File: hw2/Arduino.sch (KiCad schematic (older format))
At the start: 9 parts

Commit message: Schematic almost complete
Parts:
- added C? (x5): C, symbol C
- added D? (x2): LED, symbol LED
- added F?: Fuse, symbol Fuse
- added P?: USB_B, symbol USB_B
- added P? (x2): CONN_01X12, symbol CONN_01X12
- added R? (x5): R, symbol R
- added U?: ATmega32U4, symbol ATmega32U4
- gave numbers to parts that had none: 9
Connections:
- net GND: now also C?.2, C?.2, C?.2, C?.2, C?.2, P?.10 (P10), P?.2 (P2), P?.4 (GND), P?.9 (P9), U?.15 (GND), U?.23 (GND), U?.33 ((~HWB~)PE2), U?.35 (GND), U?.43 (GND)
- net VCC: now also D?.2 (A), D?.2 (A), P?.4 (P4), R?.1, U?.14 (VCC), U?.24 (AVCC), U?.34 (VCC), U?.44 (AVCC)
- net at JP1.1: now also F?.1; no longer D1.2 (A)
- new net: R?.2, U?.13 (RESET)
- new net: C?.1, U?.16 (XTAL2)
- new net: C?.1, U?.17 (XTAL1)
- new net: R?.1, U?.22 ((XCK1/~CTS~)PD5)
- new net: C?.1, U?.42 (AREF)
- new net: C?.1, U?.6 (UCAP)
- new net: D?.1 (K), R?.2 (x2)
- new net: P?.2 (D-), R?.2
- new net: P?.3 (D+), R?.2
- new net A0: P?.8 (P8), U?.36 ((ADC7/TDI)PF7)
- new net A1: P?.7 (P7), U?.37 ((ADC6/TDO)PF6)
- new net A2: P?.6 (P6), U?.38 ((ADC5/TMS)PF5)
- new net A3: P?.5 (P5), U?.39 ((ADC4/TCK)PF4)
- new net A4: U?.40 ((ADC1)PF1)
- new net A5: U?.41 ((ADC0)PF0)
- new net D+: R?.1
- new net D-: R?.1
- new net D10: P?.12 (P12), U?.30 ((ADC13/OC1B/OC4B/PCINT13)PB6)
- new net D11: U?.12 ((OC0A/OC1C/~RTS~/PCINT7)PB7)
- new net D12: U?.26 ((T1/~OC4D~/ADC9)PD6)
- new net D13: U?.32 ((ICP3/CLK0/OC4A)PC7)
- new net D14: R?.1, U?.8 ((SS/PCINT0)PB0)
- new net D2: P?.8 (P8), U?.19 ((SDA/INT1)PD1)
- new net D3: P?.7 (P7), U?.18 ((OC0B/SCL/INT0)PD0)
- new net D4: P?.6 (P6), U?.25 ((ICP2/ADC8)PD4)
- new net D5: P?.5 (P5), U?.31 ((OC3A/~OC4A~)PC6)
- new net D6: P?.4 (P4), U?.27 ((T0/OC4D/ADC10)PD7)
- new net D7: P?.3 (P3), U?.1 ((INT6/AIN0)PE6)
- new net D8: P?.2 (P2), U?.28 ((ADC11/PCINT4)PB4)
- new net D9: P?.1 (P1), U?.29 ((ADC12/OC1A/~OC4B~/PCINT12)PB5)
- new net MISO: P?.10 (P10), U?.11 ((PDO/MISO/PCINT3)PB3)
- new net MOSI: P?.11 (P11), U?.10 ((PDI/MOSI/PCINT2)PB2)
- new net RESET: P?.3 (P3)
- new net RXI: P?.11 (P11), U?.20 ((RXD/INT2)PD2)
- new net SCK: P?.9 (P9), U?.9 ((SCLK/PCINT1)PB1)
- new net TX0: P?.12 (P12)
- new net TXD: U?.21 ((TXD/INT3)PD3)
- new net UVCC: C?.1, F?.2, P?.1 (VBUS), U?.2 (UVCC)
- no-connect marks 1 -> 2

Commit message: Schema footprint association almost finalized
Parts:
- added 16MHz1: Crystal_Small, Crystals:Crystal_AT310_d3.0mm_l10.0mm_Horizontal, symbol Crystal_Small
- added P1: CONN_01X02, Socket_Strips:Socket_Strip_Angled_1x02_Pitch2.00mm, symbol CONN_01X02
- 0,1uF1: renamed from C4; footprint (none) -> Capacitors_SMD:C_0805
- 0,1uF2, 1uF2, 1uF3, 22pF1, 22pF2: renamed from C?; footprint (none) -> Capacitors_SMD:C_0805
- 10K1, R1, R2: renamed from R?; footprint (none) -> Resistors_SMD:R_0805
- 10uF1: renamed from C1; footprint (none) -> Capacitors_SMD:CP_Elec_3x5.3
- 10uF2: renamed from C2; footprint (none) -> Capacitors_SMD:CP_Elec_3x5.3
- 1K1: renamed from R1; footprint (none) -> Resistors_SMD:R_0805
- 1uF1: renamed from C3; footprint (none) -> Capacitors_SMD:C_0805
- 500mA1: renamed from F?; footprint (none) -> Fuse_Holders_and_Fuses:Fuse_SMD1206_HandSoldering
- D1: footprint (none) -> Diodes_SMD:D_0805
- D2: renamed from D?; value LED -> Yellow; footprint (none) -> LEDs:LED_0805
- D3: renamed from D?; value LED -> Green; footprint (none) -> LEDs:LED_0805
- JP1: footprint (none) -> Pin_Headers:Pin_Header_Straight_1x02_Pitch1.27mm
- P2, P3: renamed from P?; footprint (none) -> Pin_Headers:Pin_Header_Straight_1x12_Pitch1.27mm
- P4: renamed from P?; footprint (none) -> Connectors:USB_B
- R3, R4: renamed from R?; value R -> 330; footprint (none) -> Resistors_SMD:R_0805
- Red1: renamed from D2; footprint (none) -> LEDs:LED_0805
- U1: footprint (none) -> TO_SOT_Packages_SMD:SOT-23
- gave numbers to parts that had none: 1
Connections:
- net D+: now also U2.4 (D+)
- net D-: now also U2.3 (D-)
- net GND: now also U2.5 (UGND), P1.1 (P1)
- net UVCC: now also U2.7 (VBUS)
- net VCC: now also P1.2 (P2)
- net at 22pF2.1, U2.16 (XTAL2): now also 16MHz1.2
- net at 22pF1.1, U2.17 (XTAL1): now also 16MHz1.1

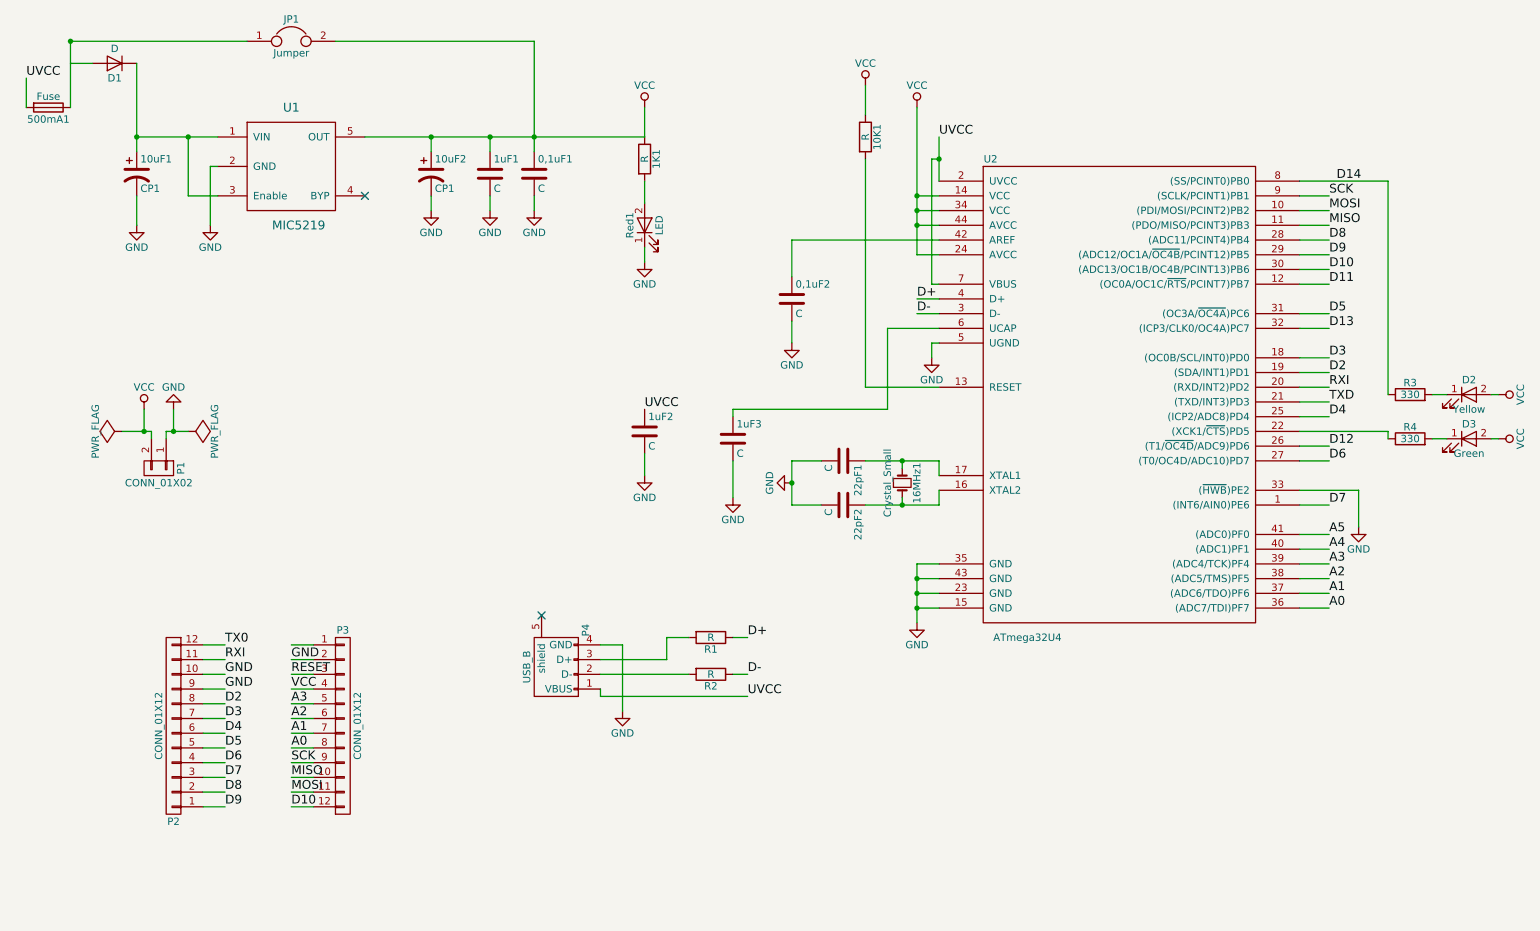
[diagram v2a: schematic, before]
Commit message: Corrections in schema; pcb layout implementation initialized
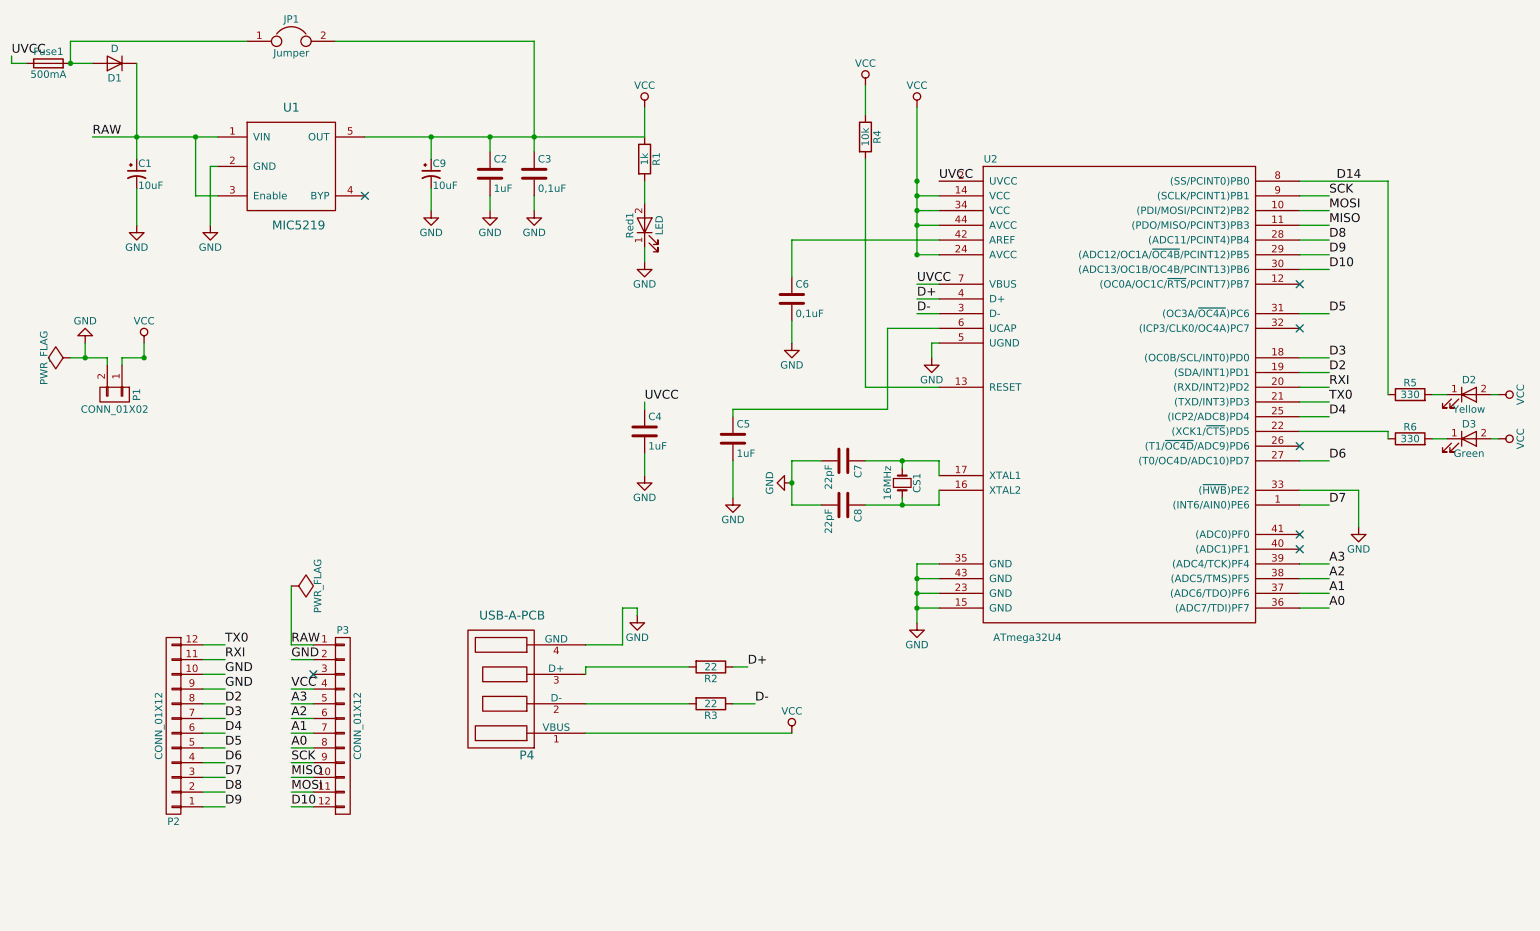
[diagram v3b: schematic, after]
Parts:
- removed 10uF1, 10uF2: CP1, Capacitors_SMD:CP_Elec_3x5.3, symbol CP1
- removed P4: USB_B, Connectors:USB_B, symbol USB_B
- added C1, C9: 10uF, Capacitors_SMD:CP_Elec_3x5.3, symbol CP1_Small
- added P4: USB-A-PCB, Connectors:USB_A, symbol USB-A-PCB
- C2: renamed from 1uF1; value C -> 1uF
- C3: renamed from 0,1uF1; value C -> 0,1uF
- C4: renamed from 1uF2; value C -> 1uF
- C5: renamed from 1uF3; value C -> 1uF
- C6: renamed from 0,1uF2; value C -> 0,1uF
- C7: renamed from 22pF1; value C -> 22pF
- C8: renamed from 22pF2; value C -> 22pF
- CS1: renamed from 16MHz1; value Crystal_Small -> 16MHz
- Fuse1: renamed from 500mA1; value Fuse -> 500mA
- R1: renamed from 1K1; value R -> 1k
- R2: renamed from R1; value R -> 22
- R3: renamed from R2; value R -> 22
- R4: renamed from 10K1; value R -> 10k
- U2: footprint (none) -> Housings_QFP:LQFP-44_10x10mm_Pitch0.8mm
- renumbered R3 to R5, R4 to R6
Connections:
- net TXD is gone; now on net TX0: U2.21 ((TXD/INT3)PD3)
- net GND: now also P1.2 (P2), C1.2, C9.2, P4.4 (GND); no longer P1.1 (P1)
- net UVCC: now also Fuse1.1; no longer Fuse1.2
- net VCC: now also P1.1 (P1), C9.1, P4.1 (VBUS); no longer P1.2 (P2)
- net RAW: now reaches D1.1 (K), U1.1 (VIN), U1.3 (Enable)
- net RAW: now also P3.1 (P1), C1.1
- net at JP1.1: now also D1.2 (A), Fuse1.2; no longer Fuse1.1
- net at R3.2: now also P4.2 (D-)
- net at R2.2: now also P4.3 (D+)
- net A4: no longer names the net of U2.40 ((ADC1)PF1)
- net A5: no longer names the net of U2.41 ((ADC0)PF0)
- net D11: no longer names the net of U2.12 ((OC0A/OC1C/~RTS~/PCINT7)PB7)
- net D12: no longer names the net of U2.26 ((T1/~OC4D~/ADC9)PD6)
- net D13: no longer names the net of U2.32 ((ICP3/CLK0/OC4A)PC7)
- net RESET: no longer names the net of P3.3 (P3)
- no-connect marks 2 -> 7
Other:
- moved on the sheet: Fuse1, R2, R3

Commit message: Routing finalized
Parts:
- removed P4: USB-A-PCB, Connectors:USB_A, symbol USB-A-PCB
- added CONN1: MICRO_USB, symbol MICRO_USB
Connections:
- net GND: now also CONN1.5 (GND)
- net VCC: now also CONN1.1 (VBUS)
- net at R2.2: now also CONN1.3 (D+)
- net at R3.2: now also CONN1.2 (D-)
- no-connect marks 7 -> 9
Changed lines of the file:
@@
 LIBS:contrib
 LIBS:valves
-LIBS:usb-a-pcb
-LIBS:NorBot
+LIBS:_connectors
 LIBS:cvra
-LIBS:_connectors
+LIBS:ATMEGA32U4-AU
 LIBS:_antenna
 LIBS:_audio
@@
 LIBS:National
 LIBS:phoenix
+LIBS:NorBot
 LIBS:Arduino-cache
 EELAYER 25 0
@@
 $EndComp
 $Comp
-L GND #PWR01
+L GND #PWR5
 U 1 1 58A35B7E
 P 3450 2000
-F 0 "#PWR01" H 3450 1750 50  0001 C CNN
+F 0 "#PWR5" H 3450 1750 50  0001 C CNN
 F 1 "GND" H 3450 1850 50  0000 C CNN
 F 2 "" H 3450 2000 50  0000 C CNN
@@
 $EndComp
 $Comp
-L GND #PWR02
+L GND #PWR6
 U 1 1 58A35BAD
 P 3850 2000
-F 0 "#PWR02" H 3850 1750 50  0001 C CNN
+F 0 "#PWR6" H 3850 1750 50  0001 C CNN
 F 1 "GND" H 3850 1850 50  0000 C CNN
 F 2 "" H 3850 2000 50  0000 C CNN
@@
 $EndComp
 $Comp
-L GND #PWR03
+L GND #PWR7
 U 1 1 58A35BDC
 P 4150 2000
-F 0 "#PWR03" H 4150 1750 50  0001 C CNN
+F 0 "#PWR7" H 4150 1750 50  0001 C CNN
 F 1 "GND" H 4150 1850 50  0000 C CNN
 F 2 "" H 4150 2000 50  0000 C CNN
@@
 NoConn ~ 3000 1900
 $Comp
-L GND #PWR04
+L GND #PWR10
 U 1 1 58A35CC6
 P 4900 2350
-F 0 "#PWR04" H 4900 2100 50  0001 C CNN
+F 0 "#PWR10" H 4900 2100 50  0001 C CNN
 F 1 "GND" H 4900 2200 50  0000 C CNN
 F 2 "" H 4900 2350 50  0000 C CNN
@@
 $EndComp
 $Comp
-L GND #PWR05
+L GND #PWR2
 U 1 1 58A35D47
 P 1450 2100
-F 0 "#PWR05" H 1450 1850 50  0001 C CNN
+F 0 "#PWR2" H 1450 1850 50  0001 C CNN
 F 1 "GND" H 1450 1950 50  0000 C CNN
 F 2 "" H 1450 2100 50  0000 C CNN
@@
 $EndComp
 $Comp
-L GND #PWR06
+L GND #PWR4
 U 1 1 58A35D76
 P 1950 2100
-F 0 "#PWR06" H 1950 1850 50  0001 C CNN
+F 0 "#PWR4" H 1950 1850 50  0001 C CNN
 F 1 "GND" H 1950 1950 50  0000 C CNN
 F 2 "" H 1950 2100 50  0000 C CNN
@@
 $EndComp
 $Comp
-L VCC #PWR07
+L VCC #PWR9
 U 1 1 58A35EC2
 P 4900 1300
-F 0 "#PWR07" H 4900 1150 50  0001 C CNN
+F 0 "#PWR9" H 4900 1150 50  0001 C CNN
 F 1 "VCC" H 4900 1450 50  0000 C CNN
 F 2 "" H 4900 1300 50  0000 C CNN
@@
 $EndComp
 $Comp
-L GND #PWR08
+L GND #PWR11
 U 1 1 58A385E3
 P 4900 3800
-F 0 "#PWR08" H 4900 3550 50  0001 C CNN
+F 0 "#PWR11" H 4900 3550 50  0001 C CNN
 F 1 "GND" H 4900 3650 50  0000 C CNN
 F 2 "" H 4900 3800 50  0000 C CNN
@@
 $EndComp
 $Comp
-L GND #PWR09
+L GND #PWR13
 U 1 1 58A38627
 P 5900 2900
-F 0 "#PWR09" H 5900 2650 50  0001 C CNN
+F 0 "#PWR13" H 5900 2650 50  0001 C CNN
 F 1 "GND" H 5900 2750 50  0000 C CNN
 F 2 "" H 5900 2900 50  0000 C CNN
@@
 $EndComp
 $Comp
-L GND #PWR010
+L GND #PWR12
 U 1 1 58A3868B
 P 5500 3950
-F 0 "#PWR010" H 5500 3700 50  0001 C CNN
+F 0 "#PWR12" H 5500 3700 50  0001 C CNN
 F 1 "GND" H 5500 3800 50  0000 C CNN
 F 2 "" H 5500 3950 50  0000 C CNN
@@
 $EndComp
 $Comp
-L GND #PWR011
+L GND #PWR14
 U 1 1 58A386CF
 P 5900 3850
-F 0 "#PWR011" H 5900 3600 50  0001 C CNN
+F 0 "#PWR14" H 5900 3600 50  0001 C CNN
 F 1 "GND" H 5900 3700 50  0000 C CNN
 F 2 "" H 5900 3850 50  0000 C CNN
@@
 $EndComp
 $Comp
-L VCC #PWR012
+L VCC #PWR16
 U 1 1 58A38733
 P 6400 1150
-F 0 "#PWR012" H 6400 1000 50  0001 C CNN
+F 0 "#PWR16" H 6400 1000 50  0001 C CNN
 F 1 "VCC" H 6400 1300 50  0000 C CNN
 F 2 "" H 6400 1150 50  0000 C CNN
@@
 $EndComp
 $Comp
-L VCC #PWR013
+L VCC #PWR17
 U 1 1 58A38797
 P 6750 1300
-F 0 "#PWR013" H 6750 1150 50  0001 C CNN
+F 0 "#PWR17" H 6750 1150 50  0001 C CNN
 F 1 "VCC" H 6750 1450 50  0000 C CNN
 F 2 "" H 6750 1300 50  0000 C CNN
@@
 $EndComp
 $Comp
-L GND #PWR014
+L GND #PWR18
 U 1 1 58A38EE5
 P 6750 4800
-F 0 "#PWR014" H 6750 4550 50  0001 C CNN
+F 0 "#PWR18" H 6750 4550 50  0001 C CNN
 F 1 "GND" H 6750 4650 50  0000 C CNN
 F 2 "" H 6750 4800 50  0000 C CNN
@@
 $EndComp
 $Comp
-L GND #PWR015
+L GND #PWR20
 U 1 1 58A39270
 P 9750 4150
-F 0 "#PWR015" H 9750 3900 50  0001 C CNN
+F 0 "#PWR20" H 9750 3900 50  0001 C CNN
 F 1 "GND" H 9750 4000 50  0000 C CNN
 F 2 "" H 9750 4150 50  0000 C CNN
@@
 $EndComp
 $Comp
-L VCC #PWR016
+L VCC #PWR22
 U 1 1 58A3971C
 P 10700 3550
-F 0 "#PWR016" H 10700 3400 50  0001 C CNN
+F 0 "#PWR22" H 10700 3400 50  0001 C CNN
 F 1 "VCC" H 10700 3700 50  0000 C CNN
 F 2 "" H 10700 3550 50  0000 C CNN
@@
 $EndComp
 $Comp
-L VCC #PWR017
+L VCC #PWR21
 U 1 1 58A3976C
 P 10700 3250
-F 0 "#PWR017" H 10700 3100 50  0001 C CNN
+F 0 "#PWR21" H 10700 3100 50  0001 C CNN
 F 1 "VCC" H 10700 3400 50  0000 C CNN
 F 2 "" H 10700 3250 50  0000 C CNN
@@
 $EndComp
 $Comp
-L GND #PWR018
+L GND #PWR8
 U 1 1 58A3CA70
 P 4850 4750
-F 0 "#PWR018" H 4850 4500 50  0001 C CNN
+F 0 "#PWR8" H 4850 4500 50  0001 C CNN
 F 1 "GND" H 4850 4600 50  0000 C CNN
 F 2 "" H 4850 4750 50  0000 C CNN
@@
 	9350 4700 9550 4700
 Wire Wire Line
-	4500 4950 4750 4950
-Wire Wire Line
-	4750 4950 4750 4700
-Wire Wire Line
-	4500 5100 5200 5100
-Wire Wire Line
-	4500 5350 5200 5350
+	4750 6200 4750 4700
+Wire Wire Line
+	4900 5100 5200 5100
+Wire Wire Line
+	5000 5350 5200 5350
 Wire Wire Line
 	5500 5100 5600 5100
@@
 	5500 5350 5650 5350
 Wire Wire Line
-	4500 5550 5900 5550
+	5400 5550 5900 5550
 Wire Wire Line
 	1900 4950 2050 4950
@@
 	6850 2900 6850 3000
 $Comp
-L GND #PWR019
+L GND #PWR19
 U 1 1 58A4E3D9
 P 6850 3000
-F 0 "#PWR019" H 6850 2750 50  0001 C CNN
+F 0 "#PWR19" H 6850 2750 50  0001 C CNN
 F 1 "GND" H 6850 2850 50  0000 C CNN
 F 2 "" H 6850 3000 50  0000 C CNN
@@
 NoConn ~ 2650 5150
 $Comp
-L VCC #PWR020
+L VCC #PWR15
 U 1 1 58A65E09
 P 5900 5550
-F 0 "#PWR020" H 5900 5400 50  0001 C CNN
+F 0 "#PWR15" H 5900 5400 50  0001 C CNN
 F 1 "VCC" H 5900 5700 50  0000 C CNN
 F 2 "" H 5900 5550 50  0000 C CNN
@@
 	1    0    0    -1
 $EndComp
-$Comp
-L USB-A-PCB P4
-U 1 1 58A65FC7
-P 4100 5250
-F 0 "P4" H 4100 5700 60  0000 C CNN
-F 1 "USB-A-PCB" H 4200 4750 60  0000 C CNN
-F 2 "Connectors:USB_A" H 4100 5250 60  0001 C CNN
-F 3 "" H 4100 5250 60  0001 C CNN
-	1    4100 5250
-	-1   0    0    1
-$EndComp
-Wire Wire Line
-	4500 5100 4500 5150
 Wire Wire Line
 	4850 4750 4850 4700
@@
 $EndComp
 $Comp
-L VCC #PWR021
+L VCC #PWR3
 U 1 1 58A64122
 P 1500 2900
-F 0 "#PWR021" H 1500 2750 50  0001 C CNN
+F 0 "#PWR3" H 1500 2750 50  0001 C CNN
 F 1 "VCC" H 1500 3050 50  0000 C CNN
 F 2 "" H 1500 2900 50  0000 C CNN
@@
 $EndComp
 $Comp
-L PWR_FLAG #FLG022
+L PWR_FLAG #FLG2
 U 1 1 58A6418A
 P 2500 4550
-F 0 "#FLG022" H 2500 4645 50  0001 C CNN
+F 0 "#FLG2" H 2500 4645 50  0001 C CNN
 F 1 "PWR_FLAG" H 2500 4730 50  0000 C CNN
 F 2 "" H 2500 4550 50  0000 C CNN
@@
 $EndComp
 $Comp
-L PWR_FLAG #FLG023
+L PWR_FLAG #FLG1
 U 1 1 58A641F2
 P 1000 3000
-F 0 "#FLG023" H 1000 3095 50  0001 C CNN
+F 0 "#FLG1" H 1000 3095 50  0001 C CNN
 F 1 "PWR_FLAG" H 1000 3180 50  0000 C CNN
 F 2 "" H 1000 3000 50  0000 C CNN
@@
 $EndComp
 $Comp
-L GND #PWR024
+L GND #PWR1
 U 1 1 58A6425A
 P 1100 2900
-F 0 "#PWR024" H 1100 2650 50  0001 C CNN
+F 0 "#PWR1" H 1100 2650 50  0001 C CNN
 F 1 "GND" H 1100 2750 50  0000 C CNN
 F 2 "" H 1100 2900 50  0000 C CNN
@@
 Text Label 4900 3300 0    60   ~ 0
 UVCC
+$Comp
+L MICRO_USB CONN1
+U 1 1 58A8FD50
+P 3950 6350
+F 0 "CONN1" H 3950 6750 60  0000 C CNN
+F 1 "MICRO_USB" H 4000 5950 60  0000 C CNN
+F 2 "" H 3950 6350 60  0000 C CNN
+F 3 "" H 3950 6350 60  0000 C CNN
+	1    3950 6350
+	-1   0    0    1
+$EndComp
+Wire Wire Line
+	4300 6400 4900 6400
+Wire Wire Line
+	4900 6400 4900 5100
+Connection ~ 4900 5100
+Wire Wire Line
+	4300 6500 5000 6500
+Wire Wire Line
+	5000 6500 5000 5350
+Connection ~ 5000 5350
+Wire Wire Line
+	4300 6600 5400 6600
+Wire Wire Line
+	5400 6600 5400 5550
+Connection ~ 5400 5550
+Wire Wire Line
+	4300 6200 4750 6200
+NoConn ~ 4300 6100
+NoConn ~ 4300 6300
 $EndSCHEMATC
